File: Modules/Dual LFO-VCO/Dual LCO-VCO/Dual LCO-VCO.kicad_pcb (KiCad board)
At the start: 2 copper layers, 187.8 x 128.5 mm, 153 parts, among them J1 Conn_01x08_Female, J10 PJ301M-12, J11 PJ301M-12, J12 PJ301M-12, J13 EURO_PWR_2x5, J14 Conn_01x07_Female, J15 Conn_01x07_Male, J16 Conn_01x05_Female, J17 Conn_01x05_Male, J18 Conn_01x02_Male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

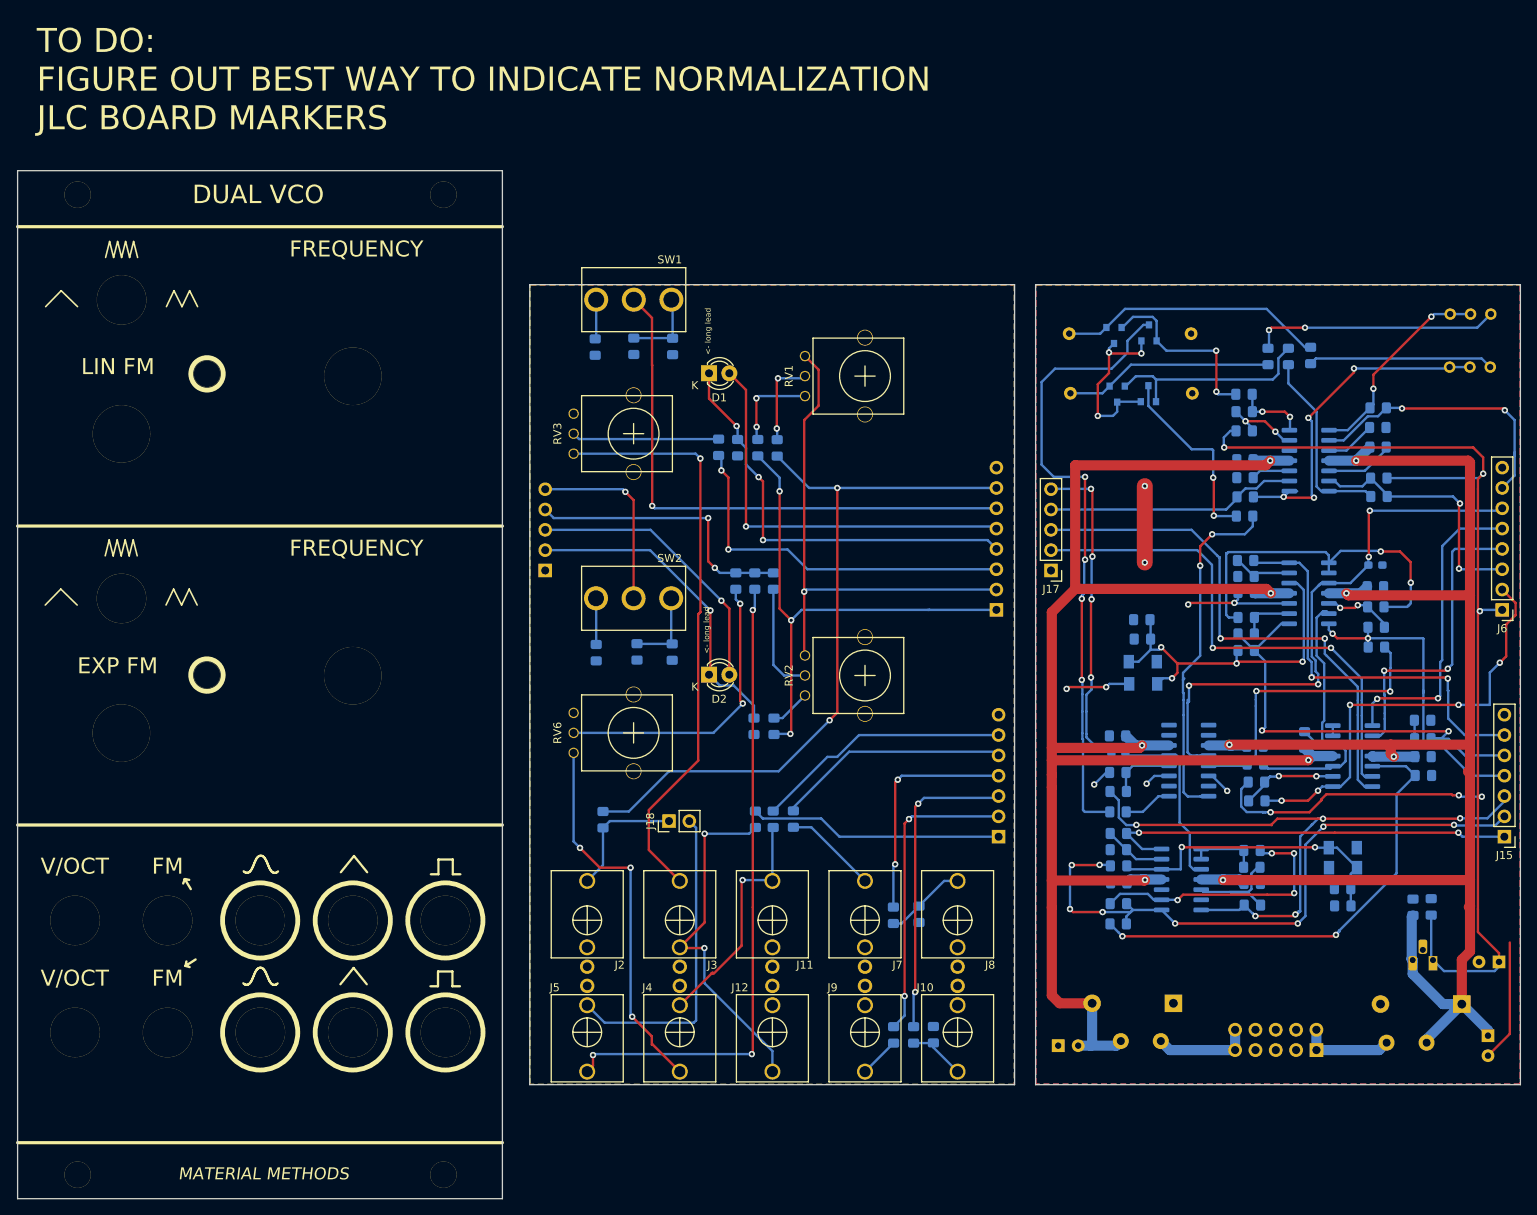
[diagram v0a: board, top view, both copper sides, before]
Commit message: Dual LFO tweaks, Trigger gen brainstorming
Dual LFO: adjusted normalization markings on the panel, added copper to panel, added JLC board markers

Brainstormed pot arrangements for random trigger module
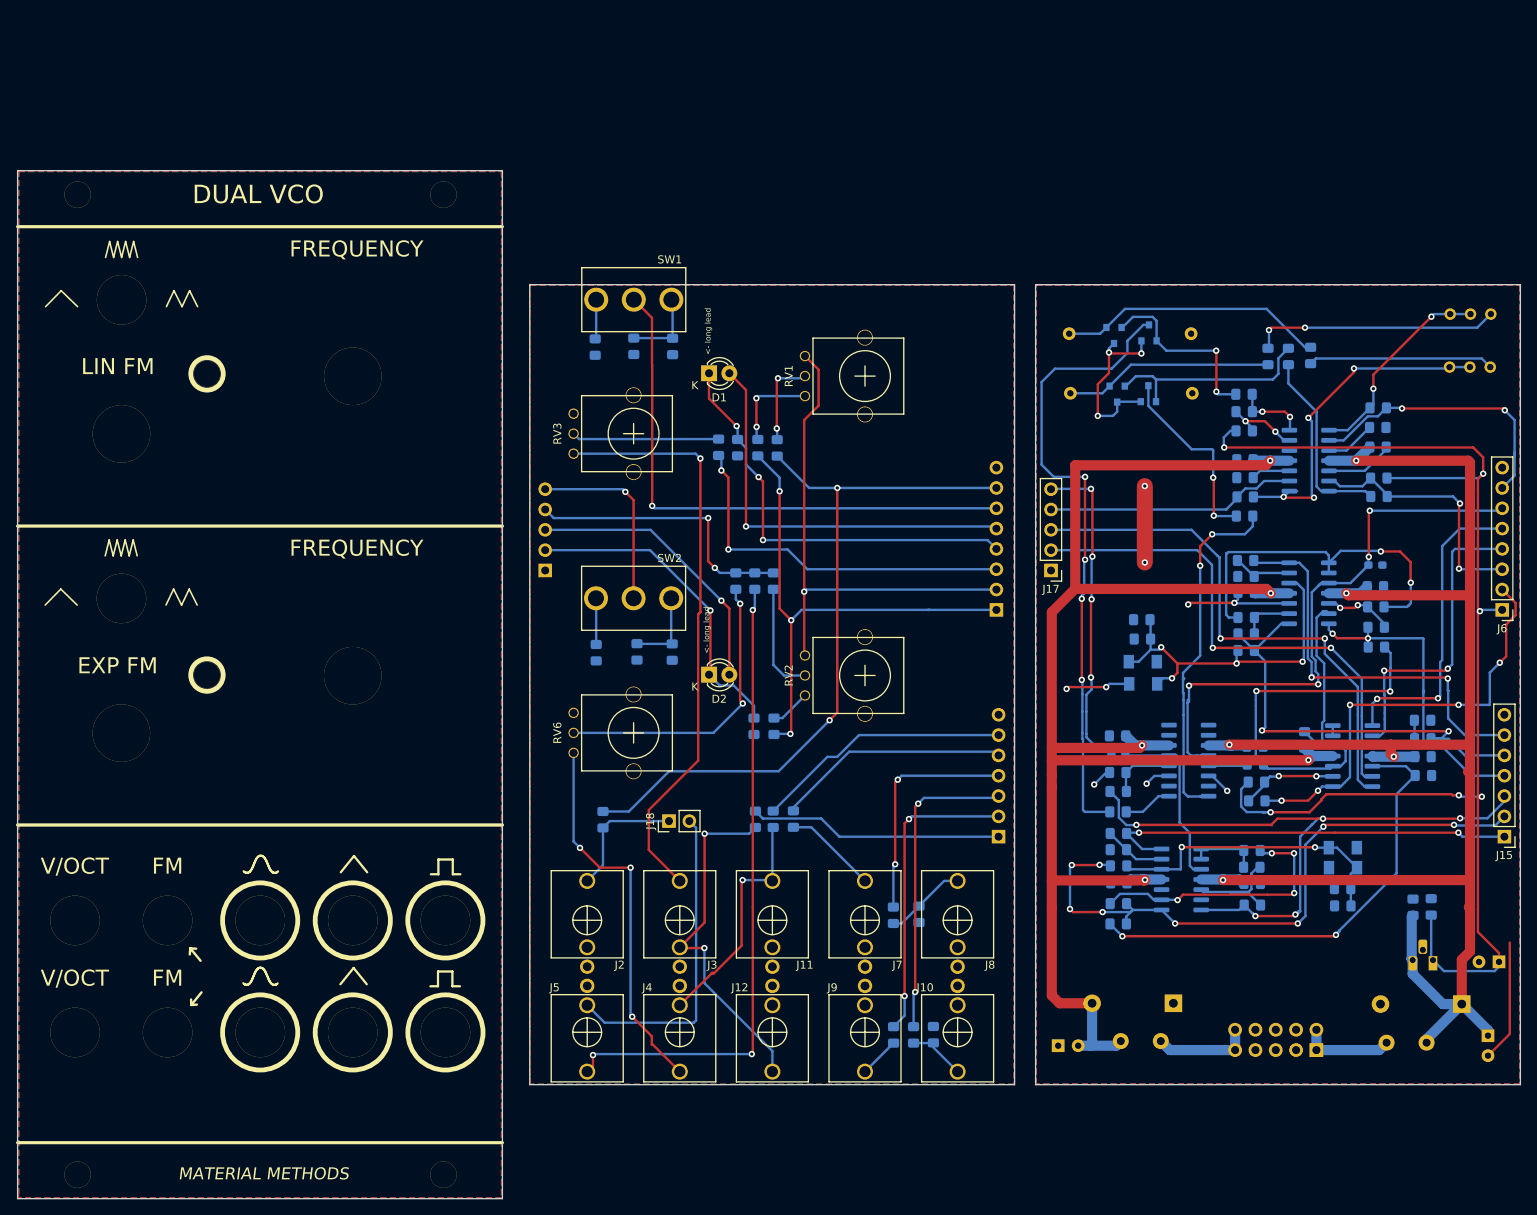
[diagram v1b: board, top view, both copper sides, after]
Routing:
- added copper zone on B.Cu, net (none)
- added copper zone on F.Cu, net (none)
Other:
- net class Default removed
- net class Power removed
- board text added: "Dual LFO v1"
- board text added: "JLCJLCJLCJLC"
- board text removed: "TO DO: FIGURE OUT BEST WAY TO INDICATE NORMALIZATION JLC BOARD MARKERS"
